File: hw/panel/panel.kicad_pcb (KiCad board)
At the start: 2 copper layers, 200 x 100 mm, 136 parts, among them J1 Barrel_Jack, J2 Conn_Coaxial, J3 Conn_ST_STDC14, Q1 BS170F, U1 STM32G031K8Tx, U2 AMS1117-3.3, U3 RFM69HW, Y1 32.768KHz

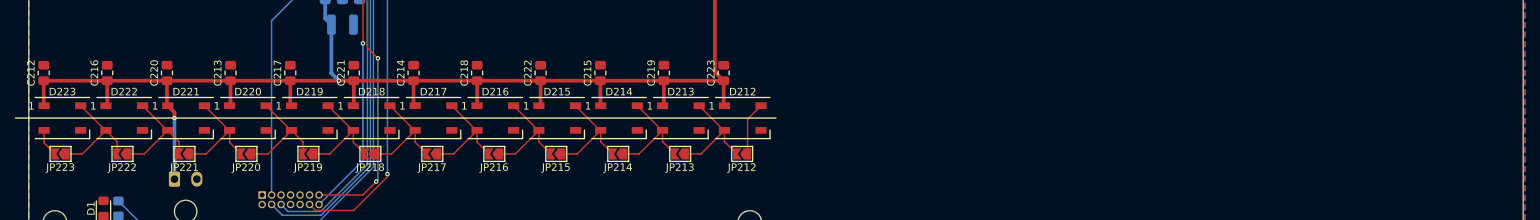
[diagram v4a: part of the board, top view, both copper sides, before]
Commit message: Added bot right
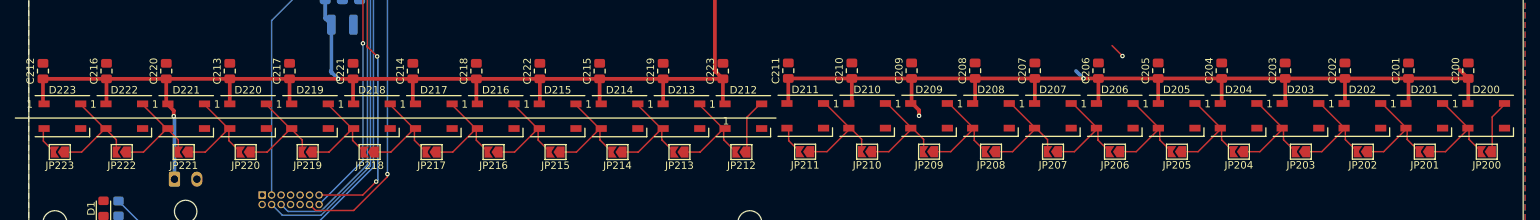
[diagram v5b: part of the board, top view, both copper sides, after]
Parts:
- added C200: 100nF, Capacitor_SMD:C_0805_2012Metric_Pad1.18x1.45mm_HandSolder, F.Cu at (253.7, 120.7)
- added C201: 100nF, Capacitor_SMD:C_0805_2012Metric_Pad1.18x1.45mm_HandSolder, F.Cu at (245.7, 120.7)
- added C202: 100nF, Capacitor_SMD:C_0805_2012Metric_Pad1.18x1.45mm_HandSolder, F.Cu at (237.2, 120.7)
- added C203: 100nF, Capacitor_SMD:C_0805_2012Metric_Pad1.18x1.45mm_HandSolder, F.Cu at (229.2, 120.7)
- added C204: 100nF, Capacitor_SMD:C_0805_2012Metric_Pad1.18x1.45mm_HandSolder, F.Cu at (220.7, 120.7)
- added C205: 100nF, Capacitor_SMD:C_0805_2012Metric_Pad1.18x1.45mm_HandSolder, F.Cu at (212.2, 120.7)
- added C206: 100nF, Capacitor_SMD:C_0805_2012Metric_Pad1.18x1.45mm_HandSolder, F.Cu at (204.2, 120.7)
- added C207: 100nF, Capacitor_SMD:C_0805_2012Metric_Pad1.18x1.45mm_HandSolder, F.Cu at (195.7, 120.7)
- added C208: 100nF, Capacitor_SMD:C_0805_2012Metric_Pad1.18x1.45mm_HandSolder, F.Cu at (187.7, 120.7)
- added C209: 100nF, Capacitor_SMD:C_0805_2012Metric_Pad1.18x1.45mm_HandSolder, F.Cu at (179.2, 120.7)
- added C210: 100nF, Capacitor_SMD:C_0805_2012Metric_Pad1.18x1.45mm_HandSolder, F.Cu at (171.2, 120.7)
- added C211: 100nF, Capacitor_SMD:C_0805_2012Metric_Pad1.18x1.45mm_HandSolder, F.Cu at (162.7, 120.7)
- added D200: WS2812B, LED_SMD:LED_WS2812B_PLCC4_5.0x5.0mm_P3.2mm, F.Cu at (256.1, 126.7)
- added D201: WS2812B, LED_SMD:LED_WS2812B_PLCC4_5.0x5.0mm_P3.2mm, F.Cu at (247.8, 126.7)
- added D202: WS2812B, LED_SMD:LED_WS2812B_PLCC4_5.0x5.0mm_P3.2mm, F.Cu at (239.5, 126.7)
- added D203: WS2812B, LED_SMD:LED_WS2812B_PLCC4_5.0x5.0mm_P3.2mm, F.Cu at (231.2, 126.7)
- added D204: WS2812B, LED_SMD:LED_WS2812B_PLCC4_5.0x5.0mm_P3.2mm, F.Cu at (222.9, 126.7)
- added D205: WS2812B, LED_SMD:LED_WS2812B_PLCC4_5.0x5.0mm_P3.2mm, F.Cu at (214.6, 126.7)
- added D206: WS2812B, LED_SMD:LED_WS2812B_PLCC4_5.0x5.0mm_P3.2mm, F.Cu at (206.3, 126.7)
- added D207: WS2812B, LED_SMD:LED_WS2812B_PLCC4_5.0x5.0mm_P3.2mm, F.Cu at (198.1, 126.7)
- added D208: WS2812B, LED_SMD:LED_WS2812B_PLCC4_5.0x5.0mm_P3.2mm, F.Cu at (189.8, 126.7)
- added D209: WS2812B, LED_SMD:LED_WS2812B_PLCC4_5.0x5.0mm_P3.2mm, F.Cu at (181.5, 126.7)
- added D210: WS2812B, LED_SMD:LED_WS2812B_PLCC4_5.0x5.0mm_P3.2mm, F.Cu at (173.2, 126.7)
- added D211: WS2812B, LED_SMD:LED_WS2812B_PLCC4_5.0x5.0mm_P3.2mm, F.Cu at (164.9, 126.7)
- added JP200: SolderJumper_2_Open, Jumper:SolderJumper-2_P1.3mm_Open_TrianglePad1.0x1.5mm, F.Cu at (256.1, 131.5)
- added JP201: SolderJumper_2_Open, Jumper:SolderJumper-2_P1.3mm_Open_TrianglePad1.0x1.5mm, F.Cu at (247.8, 131.5)
- added JP202: SolderJumper_2_Open, Jumper:SolderJumper-2_P1.3mm_Open_TrianglePad1.0x1.5mm, F.Cu at (239.5, 131.5)
- added JP203: SolderJumper_2_Open, Jumper:SolderJumper-2_P1.3mm_Open_TrianglePad1.0x1.5mm, F.Cu at (231.2, 131.5)
- added JP204: SolderJumper_2_Open, Jumper:SolderJumper-2_P1.3mm_Open_TrianglePad1.0x1.5mm, F.Cu at (223.0, 131.5)
- added JP205: SolderJumper_2_Open, Jumper:SolderJumper-2_P1.3mm_Open_TrianglePad1.0x1.5mm, F.Cu at (214.7, 131.5)
- added JP206: SolderJumper_2_Open, Jumper:SolderJumper-2_P1.3mm_Open_TrianglePad1.0x1.5mm, F.Cu at (206.4, 131.5)
- added JP207: SolderJumper_2_Open, Jumper:SolderJumper-2_P1.3mm_Open_TrianglePad1.0x1.5mm, F.Cu at (198.1, 131.5)
- added JP208: SolderJumper_2_Open, Jumper:SolderJumper-2_P1.3mm_Open_TrianglePad1.0x1.5mm, F.Cu at (189.8, 131.5)
- added JP209: SolderJumper_2_Open, Jumper:SolderJumper-2_P1.3mm_Open_TrianglePad1.0x1.5mm, F.Cu at (181.5, 131.5)
- added JP210: SolderJumper_2_Open, Jumper:SolderJumper-2_P1.3mm_Open_TrianglePad1.0x1.5mm, F.Cu at (173.2, 131.5)
- added JP211: SolderJumper_2_Open, Jumper:SolderJumper-2_P1.3mm_Open_TrianglePad1.0x1.5mm, F.Cu at (164.9, 131.5)
- moved JP213 0.27 mm to (148.1, 131.6)
- moved JP214 0.27 mm to (139.8, 131.6)
- moved JP218 0.27 mm to (106.6, 131.6)
- moved JP219 0.27 mm to (98.3, 131.6)
- moved JP222 0.27 mm to (73.4, 131.6)
- moved C212 0.27 mm to (62.9, 120.7)
- moved C213 0.27 mm to (87.9, 120.7)
- moved C214 0.27 mm to (112.4, 120.7)
- moved C215 0.27 mm to (137.4, 120.7)
- moved C216 0.27 mm to (71.4, 120.7)
- moved C217 0.27 mm to (95.9, 120.7)
- moved C218 0.27 mm to (120.9, 120.7)
- moved C219 0.27 mm to (145.9, 120.7)
- moved C220 0.27 mm to (79.4, 120.7)
- moved C221 0.27 mm to (104.4, 120.7)
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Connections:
- net /led_top_right/RGB_OUT renamed /led_bot_right/RGB_IN
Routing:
- net +6V: track 480.1 -> 617.0 mm, vias 3 -> 5
- net Net-(D210-DOUT): track 0.00 -> 15.2 mm
- net Net-(D209-DOUT): track 0.00 -> 15.2 mm
- net Net-(D208-DOUT): track 0.00 -> 15.2 mm
- net Net-(D207-DOUT): track 0.00 -> 15.1 mm
- net Net-(D206-DOUT): track 0.00 -> 15.1 mm
- net Net-(D205-DOUT): track 0.00 -> 15.1 mm
- net Net-(D204-DOUT): track 0.00 -> 15.1 mm
- net Net-(D203-DOUT): track 0.00 -> 15.1 mm
- net Net-(D202-DOUT): track 0.00 -> 15.1 mm
- net Net-(D201-DOUT): track 0.00 -> 15.1 mm
- net Net-(D200-DOUT): track 0.00 -> 15.1 mm
- net /led_bot_right/RGB_IN: track 4.49 -> 11.7 mm
- net /led_bot_left/RGB_IN: track 7.20 -> 11.0 mm
- net /UART_RX: track 56.7 -> 58.7 mm, vias 3 -> 4
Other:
- board text added: "Barrel_Jack"

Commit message: optimized paths
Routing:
- net /led_bot_right/RGB_IN: track 11.7 -> 77.2 mm
- net /led_top_left/RGB_IN: track 11.0 -> 47.1 mm, vias 0 -> 1
- net +6V: track 617.0 -> 628.3 mm, vias 5 -> 3
- net /led_bot_left/RGB_IN: track 11.0 -> 15.6 mm
- net /led_top_left/RGB_OUT: track 13.4 -> 16.5 mm
- net /UART_RX: track 58.7 -> 56.7 mm, vias 4 -> 3

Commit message: holes
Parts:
- added H200: MountingHole, MountingHole:MountingHole_3.2mm_M3, F.Cu at (257.5, 48.0)
- added H201: MountingHole, MountingHole:MountingHole_3.2mm_M3, F.Cu at (257.5, 141.0)
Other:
- board text added: "window panel v1"
- board text removed: "win panel v1"
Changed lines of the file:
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@@
 		)
 	)
+	(footprint "MountingHole:MountingHole_3.2mm_M3"
+		(layer "F.Cu")
+		(at 257.5 141)
+		(descr "Mounting Hole 3.2mm, no annular, M3")
+		(tags "mounting hole 3.2mm no annular m3")
+		(property "Reference" "H201"
+			(at 0 -4.2 0)
+			(layer "F.SilkS")
+			(hide yes)
+			(effects
+				(font
+					(size 1 1)
+					(thickness 0.15)
+				)
+			)
+		)
+		(property "Value" "MountingHole"
+			(at 0 4.2 0)
+			(layer "F.Fab")
+			(hide yes)
+			(effects
+				(font
+					(size 1 1)
+					(thickness 0.15)
+				)
+			)
+		)
+		(property "Footprint" "MountingHole:MountingHole_3.2mm_M3"
+			(at 0 0 0)
+			(unlocked yes)
+			(layer "F.Fab")
+			(hide yes)
+			(effects
+				(font
+					(size 1.27 1.27)
+					(thickness 0.15)
+				)
+			)
+		)
+		(property "Datasheet" ""
+			(at 0 0 0)
+			(unlocked yes)
+			(layer "F.Fab")
+			(hide yes)
+			(effects
+				(font
+					(size 1.27 1.27)
+					(thickness 0.15)
+				)
+			)
+		)
+		(property "Description" "Mounting Hole without connection"
+			(at 0 0 0)
+			(unlocked yes)
+			(layer "F.Fab")
+			(hide yes)
+			(effects
+				(font
+					(size 1.27 1.27)
+					(thickness 0.15)
+				)
+			)
+		)
+		(property ki_fp_filters "MountingHole*")
+		(sheetname "Root")
+		(sheetfile "panel.kicad_sch")
+		(attr exclude_from_pos_files exclude_from_bom)
+		(fp_circle
+			(center 0 0)
+			(end 3.2 0)
+			(stroke
+				(width 0.15)
+				(type solid)
+			)
+			(fill none)
+			(layer "Cmts.User")
+		)
+		(fp_circle
+			(center 0 0)
+			(end 3.45 0)
+			(stroke
+				(width 0.05)
+				(type solid)
+			)
+			(fill none)
+			(layer "F.CrtYd")
+		)
+		(fp_text user "${REFERENCE}"
+			(at 0 0 0)
+			(layer "F.Fab")
+			(effects
+				(font
+					(size 1 1)
+					(thickness 0.15)
+				)
+			)
+		)
+		(pad "" np_thru_hole circle
+			(at 0 0)
+			(size 3.2 3.2)
+			(drill 3.2)
+			(layers "*.Cu" "*.Mask")
+		)
+	)
 	(footprint "LED_SMD:LED_WS2812B_PLCC4_5.0x5.0mm_P3.2mm"
 		(layer "F.Cu")
@@
 		)
 	)
+	(footprint "MountingHole:MountingHole_3.2mm_M3"
+		(layer "F.Cu")
+		(at 257.5 48)
+		(descr "Mounting Hole 3.2mm, no annular, M3")
+		(tags "mounting hole 3.2mm no annular m3")
+		(property "Reference" "H200"
+			(at 0 -4.2 0)
+			(layer "F.SilkS")
+			(hide yes)
+			(effects
+				(font
+					(size 1 1)
+					(thickness 0.15)
+				)
+			)
+		)
+		(property "Value" "MountingHole"
+			(at 0 4.2 0)
+			(layer "F.Fab")
+			(hide yes)
+			(effects
+				(font
+					(size 1 1)
+					(thickness 0.15)
+				)
+			)
+		)
+		(property "Footprint" "MountingHole:MountingHole_3.2mm_M3"
+			(at 0 0 0)
+			(unlocked yes)
+			(layer "F.Fab")
+			(hide yes)
+			(effects
+				(font
+					(size 1.27 1.27)
+					(thickness 0.15)
+				)
+			)
+		)
+		(property "Datasheet" ""
+			(at 0 0 0)
+			(unlocked yes)
+			(layer "F.Fab")
+			(hide yes)
+			(effects
+				(font
+					(size 1.27 1.27)
+					(thickness 0.15)
+				)
+			)
+		)
+		(property "Description" "Mounting Hole without connection"
+			(at 0 0 0)
+			(unlocked yes)
+			(layer "F.Fab")
+			(hide yes)
+			(effects
+				(font
+					(size 1.27 1.27)
+					(thickness 0.15)
+				)
+			)
+		)
+		(property ki_fp_filters "MountingHole*")
+		(sheetname "Root")
+		(sheetfile "panel.kicad_sch")
+		(attr exclude_from_pos_files exclude_from_bom)
+		(fp_circle
+			(center 0 0)
+			(end 3.2 0)
+			(stroke
+				(width 0.15)
+				(type solid)
+			)
+			(fill none)
+			(layer "Cmts.User")
+		)
+		(fp_circle
+			(center 0 0)
+			(end 3.45 0)
+			(stroke
+				(width 0.05)
+				(type solid)
+			)
+			(fill none)
+			(layer "F.CrtYd")
+		)
+		(fp_text user "${REFERENCE}"
+			(at 0 0 0)
+			(layer "F.Fab")
+			(effects
+				(font
+					(size 1 1)
+					(thickness 0.15)
+				)
+			)
+		)
+		(pad "" np_thru_hole circle
+			(at 0 0)
+			(size 3.2 3.2)
+			(drill 3.2)
+			(layers "*.Cu" "*.Mask")
+		)
+	)
 	(footprint "Jumper:SolderJumper-2_P1.3mm_Open_TrianglePad1.0x1.5mm"
 		(layer "F.Cu")
@@
 		(layer "Edge.Cuts")
 	)
-	(gr_text "win panel v1"
-		(at 138.5 142.5 0)
+	(gr_text "window panel v1"
+		(at 232.5 141.5 0)
 		(layer "F.SilkS")
 		(effects

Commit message: x
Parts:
- added R4: 680, Resistor_SMD:R_0805_2012Metric_Pad1.20x1.40mm_HandSolder, B.Cu at (242.5, 89.6)
- added R5: 680, Resistor_SMD:R_0805_2012Metric_Pad1.20x1.40mm_HandSolder, B.Cu at (242.5, 92.5)
- added R6: 680, Resistor_SMD:R_0805_2012Metric_Pad1.20x1.40mm_HandSolder, B.Cu at (242.5, 95.5)
- D1: value LED -> ~; footprint LED_SMD:LED_0805_2012Metric_Pad1.15x1.40mm_HandSolder -> panel:light_guide
- R1: value 100k -> 680
- moved D1 187.3 mm to (252.4, 92.2), turned to -90 degrees
- moved R1 177.4 mm to (242.5, 86.7), turned to 180 degrees
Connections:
- D1 pad 1: Net-(D1-K) -> GND
- D1 pad 2: +3V3 -> Net-(D1A-A)
- R1 pad 1: Net-(D1-K) -> Net-(D1A-A)
- R1 pad 2: Net-(U1-PC6) -> +3V3
- U1 pad 11: unconnected-(U1-PA4-Pad11) -> /LED_TX
- U1 pad 12: unconnected-(U1-PA5-Pad12) -> /LED_RX
- U1 pad 13: unconnected-(U1-PA6-Pad13) -> /LED_ERROR
- U1 pad 20: Net-(U1-PC6) -> unconnected-(U1-PC6-Pad20)
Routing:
- net +3V3: track 104.0 -> 241.0 mm
- net /LED_ERROR: track 0.00 -> 131.7 mm
- net /LED_TX: track 0.00 -> 131.4 mm
- net /LED_RX: track 0.00 -> 130.8 mm
- net Net-(U1-PC6): track 75.6 -> 0.00 mm
- net Net-(D1D-A): track 0.00 -> 10.0 mm, vias 0 -> 1
- net Net-(D1B-A): track 0.00 -> 9.82 mm, vias 0 -> 1
- net Net-(D1A-A): track 0.00 -> 8.43 mm, vias 0 -> 1
- net Net-(D1C-A): track 0.00 -> 8.42 mm, vias 0 -> 1
- net /RST: track 65.8 -> 64.5 mm, vias 1 -> 3
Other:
- board text removed: "Barrel_Jack"
